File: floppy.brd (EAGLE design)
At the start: 88.6 x 93.7 mm, 20 parts, among them IC1 ATTINY13-20SU, Q1 S9018

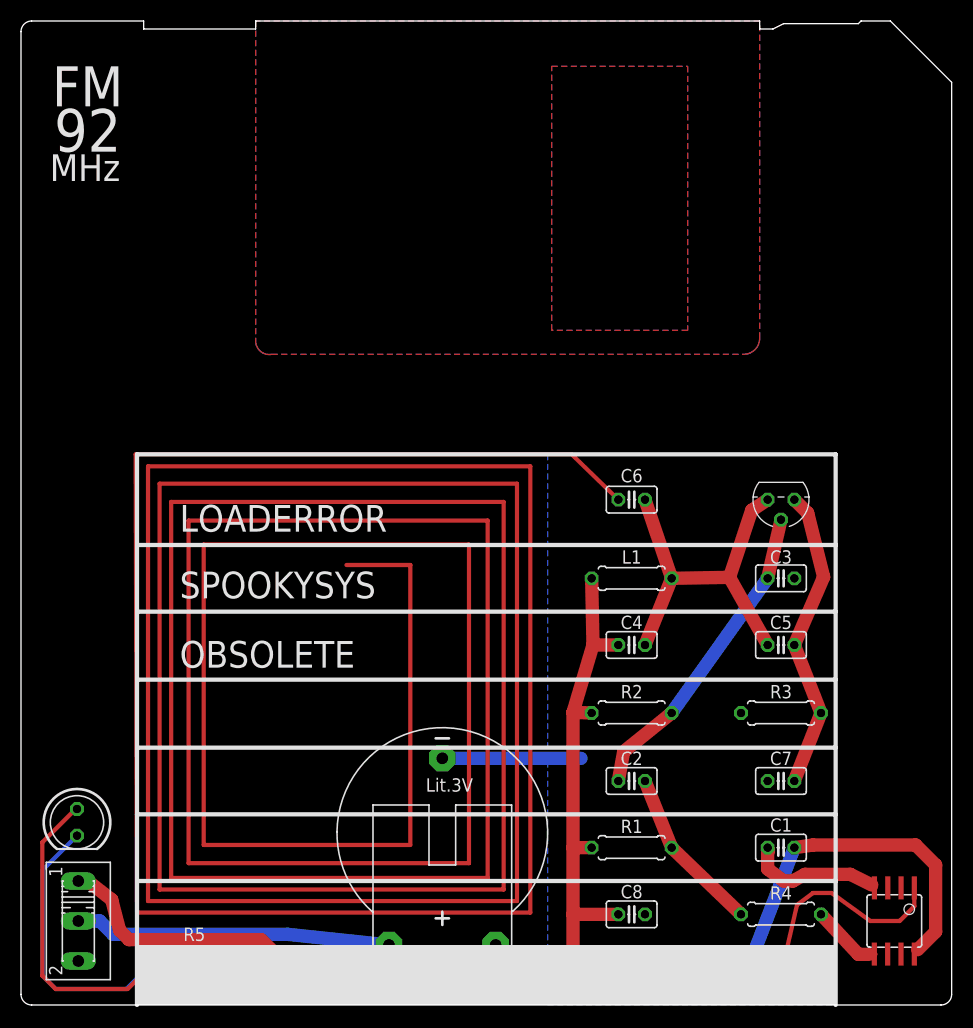
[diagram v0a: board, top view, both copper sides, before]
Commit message: Made layout much nicer LED now driven directly from AVR TODO: * check that LED can be driven driectly from AVR * pirate flag and nicer "illegal radio transmitter" text * adjust FM frequency text * check that design works in general
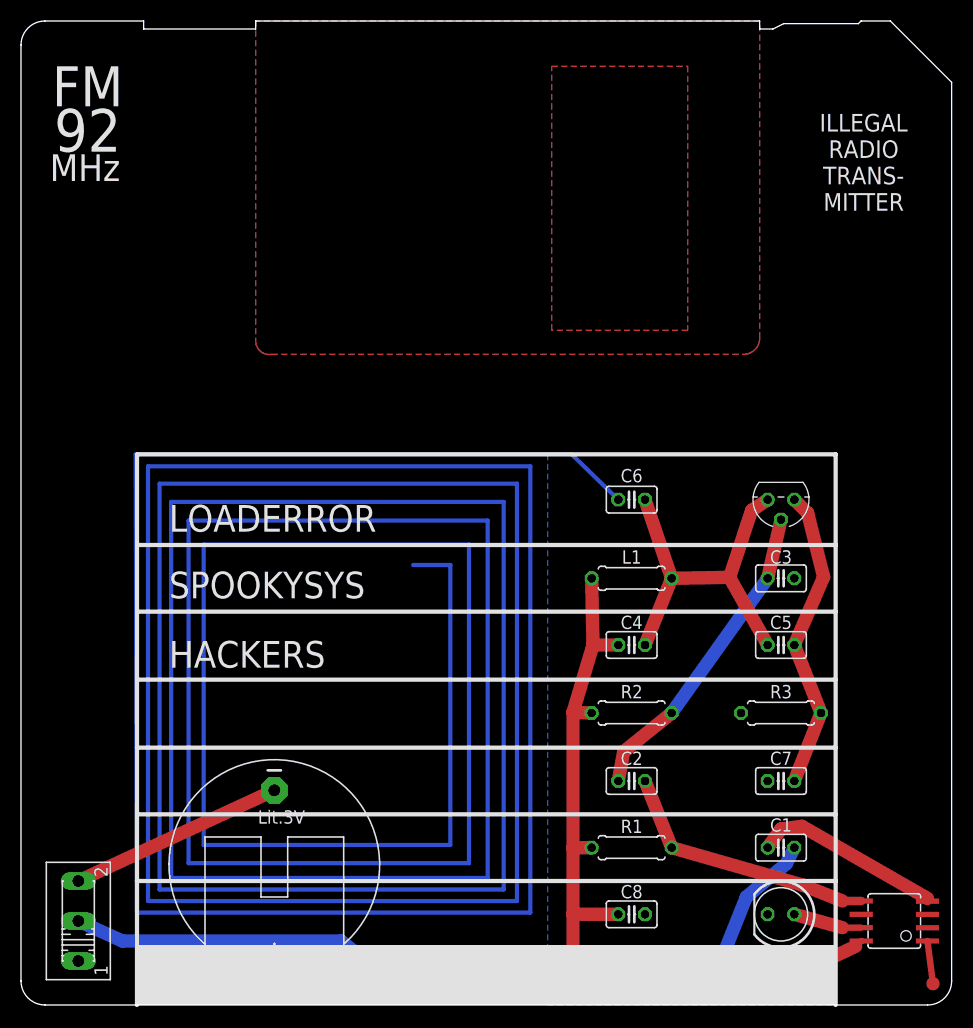
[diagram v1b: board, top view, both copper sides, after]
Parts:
- removed JP1: (no value), pinhead:1X03
- removed R4: 33, rcl:0207/7
- removed R5: 50, rcl:0207/7
- added DW: TPB1,27, testpad:B1,27
- moved LED1 67.6 mm to (72.4, 8.64), turned to 180 degrees
- moved G1 16.3 mm to (24.1, 13.5)
- turned IC1 to 90 degrees
- turned S1 to 90 degrees
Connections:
- removed net N$9: LED1.A, R5.1
- net AUDIO: now also C2.1, R1.1; no longer R4.2
- net DW: now also DW.TP; no longer JP1.2
- net GND: now also S1.2; no longer G1.-, JP1.3
- net N$3: now also G1.-, S1.3; no longer G1.+, S1.2
- net N$5: now also IC1.7, LED1.A; no longer C2.1, R1.1, R4.1
- net VCC: now also G1.+; no longer JP1.1, R5.2, S1.1
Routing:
- net VCC: track 157.9 -> 125.2 mm, vias 0 -> 1
- net N$9: track 30.3 -> 0.00 mm
- net GND: track 94.0 -> 65.2 mm
- net AUDIO: track 6.74 -> 25.7 mm
- net DW: track 21.5 -> 4.10 mm
- net N$3: track 30.2 -> 20.6 mm
- net N$5: track 16.0 -> 6.54 mm
- net ANT: track 789.9 -> 793.7 mm
- net N$4: track 32.8 -> 30.2 mm
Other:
- outline, holes or cut-outs redrawn
- board text added: "HACKERS"
- board text added: "ILLEGAL RADIO TRANS- MITTER"
- board text removed: "OBSOLETE"

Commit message: Fixed battery holder footprint Added "Illegal radio transmitter"
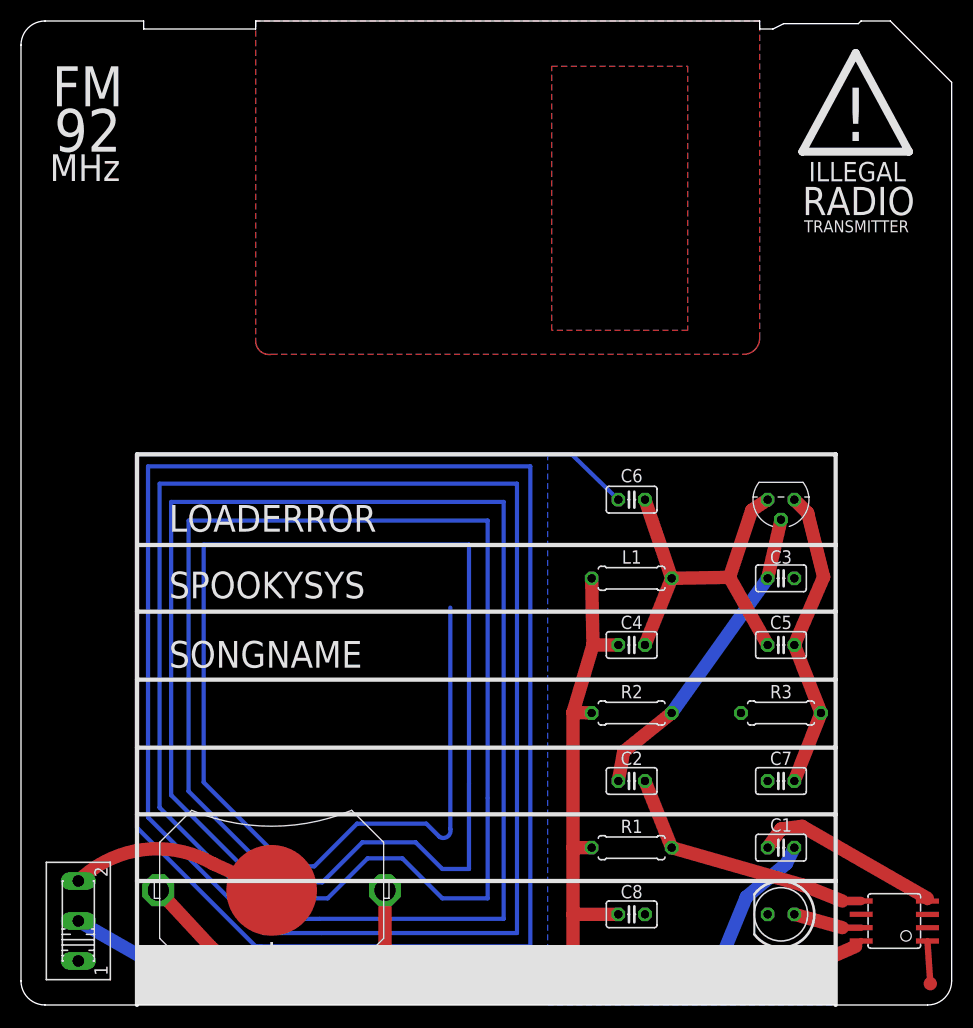
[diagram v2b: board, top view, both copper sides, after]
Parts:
- G1: value CR2032H -> BK-913; device battery:CR2032H -> local:BK-913
- moved G1 2.55 mm to (23.9, 10.9), turned to 0 degrees
- moved DW 0.25 mm to (86.6, 2.03)
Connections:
- net N$3: now also G1.V-; no longer G1.-
- net VCC: now also G1.V+1, G1.V+2; no longer G1.+
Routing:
- net N$4: track 30.2 -> 0.00 mm
- net ANT: track 793.7 -> 814.9 mm
- net VCC: track 125.2 -> 141.7 mm
- net N$3: track 20.6 -> 19.1 mm
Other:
- board text added: "!"
- board text added: "ILLEGAL"
- board text added: "RADIO"
- board text added: "SONGNAME"
- board text added: "TRANSMITTER"
- board text removed: "HACKERS"
- board text removed: "ILLEGAL RADIO TRANS- MITTER"
